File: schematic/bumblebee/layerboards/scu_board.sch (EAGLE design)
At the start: 15 parts, among them P5 B4B-EH-A, P7 B3B-EH-A

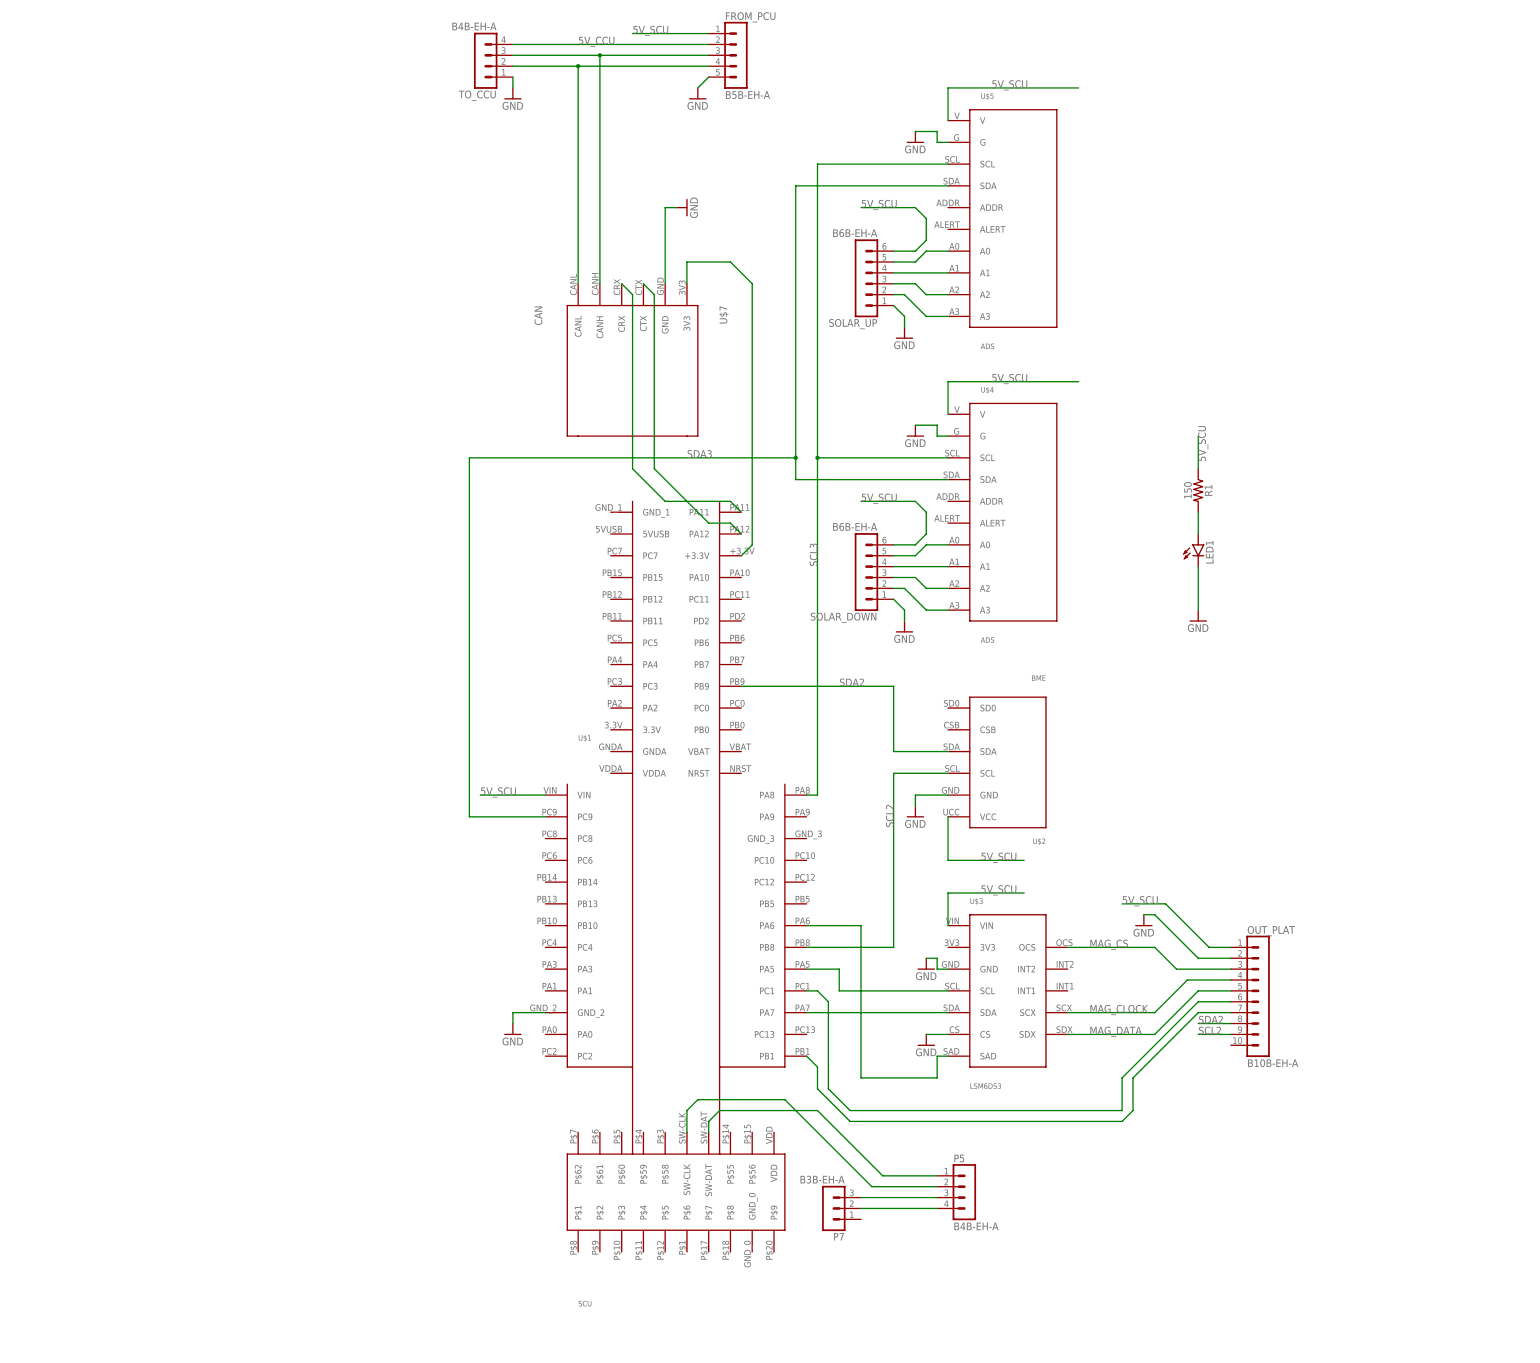
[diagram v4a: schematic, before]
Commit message: ICU готова, SCU скоро доделаю, пока что там всё не очень В либу добавлен LSM303C
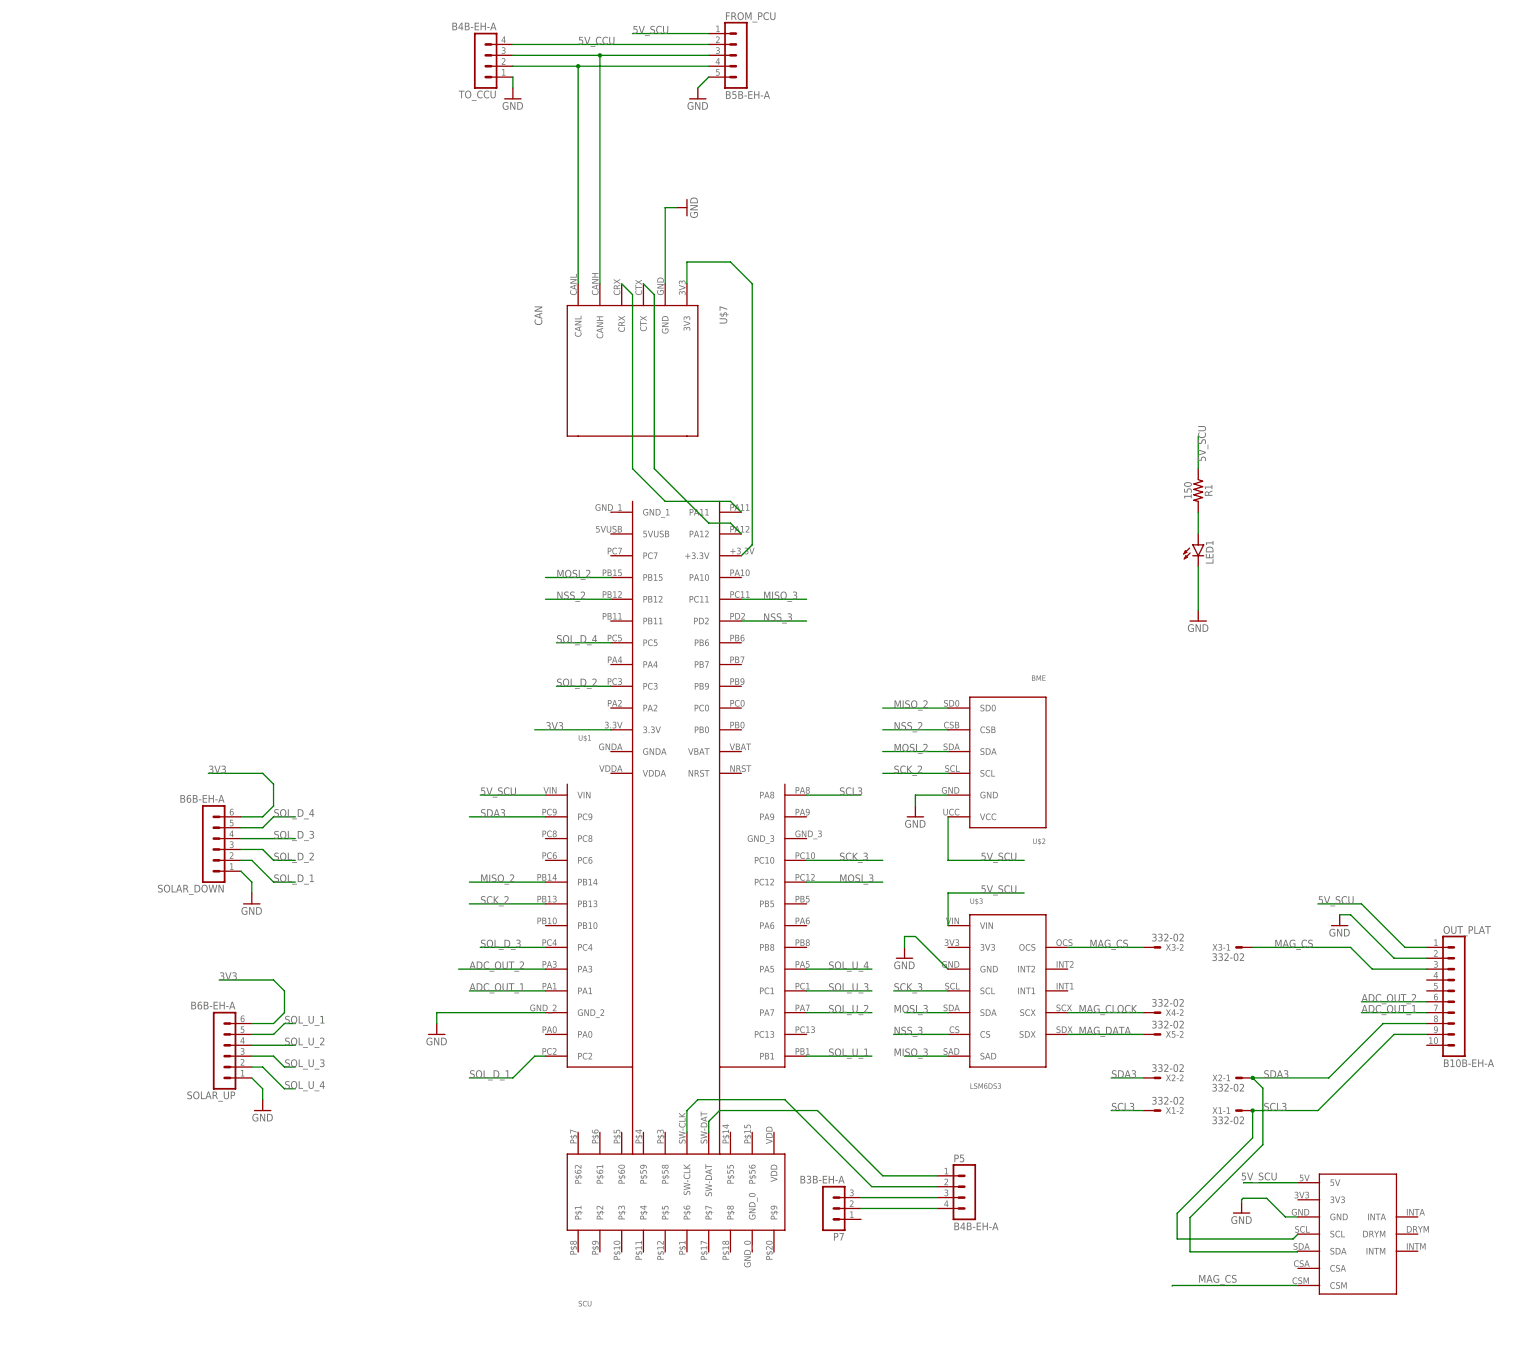
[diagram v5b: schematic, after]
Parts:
- removed U$5: ADS, bluepill:ADS
- added X1, X2, X3, X4, X5: 332-02, con-garry:332-02
- U$4: value ADS -> LSM303C; device bluepill:ADS -> bluepill:LSM303C
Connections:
- removed net N$10: SOLAR_UP.3, U$5.A2
- removed net N$11: SOLAR_UP.2, U$5.A3
- removed net N$12: SOLAR_DOWN.5, U$4.A0
- removed net N$13: SOLAR_DOWN.4, U$4.A1
- removed net N$14: SOLAR_DOWN.3, U$4.A2
- removed net N$15: SOLAR_DOWN.2, U$4.A3
- removed net N$17: OUT_PLAT.6, U$1.PC1
- removed net N$18: OUT_PLAT.7, U$1.PB1
- removed net N$2: U$1.PA5, U$3.SCL
- removed net N$3: U$1.PA6, U$3.SAD
- removed net N$4: U$1.PA7, U$3.SDA
- removed net N$8: SOLAR_UP.5, U$5.A0
- removed net N$9: SOLAR_UP.4, U$5.A1
- removed net SCL2: OUT_PLAT.9, U$1.PB8, U$2.SCL
- removed net SDA2: OUT_PLAT.8, U$1.PB9, U$2.SDA
- new net 3V3: SOLAR_DOWN.6, SOLAR_UP.6, U$1.3.3V
- new net ADC_OUT_1: OUT_PLAT.7, U$1.PA1
- new net ADC_OUT_2: OUT_PLAT.6, U$1.PA3
- new net MISO_2: U$1.PB14, U$2.SD0
- new net MISO_3: U$1.PC11, U$3.SAD
- new net MOSI_2: U$1.PB15, U$2.SDA
- new net MOSI_3: U$1.PC12, U$3.SDA
- new net NSS_2: U$1.PB12, U$2.CSB
- new net NSS_3: U$1.PD2, U$3.CS
- new net SCK_2: U$1.PB13, U$2.SCL
- new net SCK_3: U$1.PC10, U$3.SCL
- new net SOL_D_1: SOLAR_DOWN.2, U$1.PC2
- new net SOL_D_2: SOLAR_DOWN.3, U$1.PC3
- new net SOL_D_3: SOLAR_DOWN.4, U$1.PC4
- new net SOL_D_4: SOLAR_DOWN.5, U$1.PC5
- new net SOL_U_1: SOLAR_UP.5, U$1.PB1
- new net SOL_U_2: SOLAR_UP.4, U$1.PA7
- new net SOL_U_3: SOLAR_UP.3, U$1.PC1
- new net SOL_U_4: SOLAR_UP.2, U$1.PA5
- net 5V_SCU: now also U$4.5V; no longer SOLAR_DOWN.6, SOLAR_UP.6, U$4.V, U$5.V
- net GND: now also U$4.GND; no longer U$3.CS, U$4.G, U$5.G
- net MAG_CLOCK: now also X4-2.S; no longer OUT_PLAT.4
- net MAG_CS: now also U$4.CSM, X3-1.S, X3-2.S
- net MAG_DATA: now also X5-2.S; no longer OUT_PLAT.5
- net SCL3: now also OUT_PLAT.9, X1-1.S, X1-2.S; no longer U$5.SCL
- net SDA3: now also OUT_PLAT.8, X2-1.S, X2-2.S; no longer U$5.SDA
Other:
- moved on the sheet: OUT_PLAT, SOLAR_DOWN, SOLAR_UP

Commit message: Готова SCU и поправил lsm303c в либе
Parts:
- removed OUT_PLAT: B10B-EH-A, con-jst-eh:B10B-EH-A
- removed X1, X2, X3, X4, X5: 332-02, con-garry:332-02
- added P1: B8B-EH-A, con-jst-eh:B8B-EH-A
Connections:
- removed net MAG_CLOCK: U$3.SCX, X4-2.S
- removed net MAG_DATA: U$3.SDX, X5-2.S
- net 5V_SCU: now also P1.1; no longer OUT_PLAT.1
- net ADC_OUT_1: now also P1.5; no longer OUT_PLAT.7
- net ADC_OUT_2: now also P1.4; no longer OUT_PLAT.6
- net GND: now also P1.2; no longer OUT_PLAT.2
- net MAG_CS: now also P1.3; no longer OUT_PLAT.3, X3-1.S, X3-2.S
- net SCL3: now also P1.7, U$3.SCX; no longer OUT_PLAT.9, X1-1.S, X1-2.S
- net SDA3: now also P1.6, U$3.SDX; no longer OUT_PLAT.8, X2-1.S, X2-2.S

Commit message: Подготовка плат к производству
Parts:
- removed SOLAR_DOWN, SOLAR_UP: B6B-EH-A, con-jst-eh:B6B-EH-A
- added R2, R3, R4, R5, R6, R7, R8, R9: 150, SparkFun-Resistors:RESISTORAXIAL-0.3
- added SOL_D_1_2, SOL_D_3_4, SOL_U_1_2, SOL_U_3_4: B4B-EH-A, con-jst-eh:B4B-EH-A
- renumbered P1 to TO_OUT_BOARD, P5 to DEBUG, P7 to DEBUG_OUT
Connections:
- net 3V3: now also SOL_D_1_2.2, SOL_D_1_2.4, SOL_D_3_4.2, SOL_D_3_4.4, SOL_U_1_2.2, SOL_U_1_2.4, SOL_U_3_4.2, SOL_U_3_4.4; no longer SOLAR_DOWN.6, SOLAR_UP.6
- net GND: now also R2.1, R3.1, R4.2, R5.1, R6.1, R7.2, R8.2, R9.1; no longer SOLAR_DOWN.1, SOLAR_UP.1
- net SOL_D_1: now also R9.2, SOL_D_1_2.1; no longer SOLAR_DOWN.2
- net SOL_D_2: now also R8.1, SOL_D_1_2.3; no longer SOLAR_DOWN.3
- net SOL_D_3: now also R7.1, SOL_D_3_4.1; no longer SOLAR_DOWN.4
- net SOL_D_4: now also R6.2, SOL_D_3_4.3; no longer SOLAR_DOWN.5
- net SOL_U_1: now also R5.2, SOL_U_1_2.1; no longer SOLAR_UP.5
- net SOL_U_2: now also R4.1, SOL_U_1_2.3; no longer SOLAR_UP.4
- net SOL_U_3: now also R3.2, SOL_U_3_4.1; no longer SOLAR_UP.3
- net SOL_U_4: now also R2.2, SOL_U_3_4.3; no longer SOLAR_UP.2

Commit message: Платы отправлены на завод
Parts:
- renumbered U$1 to STM32H405
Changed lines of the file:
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@@
 </classes>
 <parts>
-<part name="U$1" library="bluepill" deviceset="SCU" device=""/>
+<part name="STM32H405" library="bluepill" deviceset="SCU" device=""/>
 <part name="U$2" library="bluepill" deviceset="BME" device=""/>
 <part name="GND1" library="supply1" library_urn="urn:adsk.eagle:library:371" deviceset="GND" device=""/>
@@
 </plain>
 <instances>
-<instance part="U$1" gate="G$1" x="5.08" y="2.54" smashed="yes">
+<instance part="STM32H405" gate="G$1" x="5.08" y="2.54" smashed="yes">
 <attribute name="NAME" x="-22.86" y="53.34" size="1.27" layer="95"/>
 <attribute name="VALUE" x="-22.86" y="-78.74" size="1.27" layer="96"/>
@@
 <segment>
 <pinref part="GND2" gate="1" pin="GND"/>
-<pinref part="U$1" gate="G$1" pin="GND_2"/>
+<pinref part="STM32H405" gate="G$1" pin="GND_2"/>
 <wire x1="-55.88" y1="-12.7" x2="-55.88" y2="-10.16" width="0.1524" layer="91"/>
 <wire x1="-55.88" y1="-10.16" x2="-30.48" y2="-10.16" width="0.1524" layer="91"/>
@@
 </segment>
 <segment>
-<pinref part="U$1" gate="G$1" pin="VIN"/>
+<pinref part="STM32H405" gate="G$1" pin="VIN"/>
 <wire x1="-30.48" y1="40.64" x2="-45.72" y2="40.64" width="0.1524" layer="91"/>
 <label x="-45.72" y="40.64" size="1.778" layer="95"/>
@@
 <net name="SCL3" class="0">
 <segment>
-<pinref part="U$1" gate="G$1" pin="PA8"/>
+<pinref part="STM32H405" gate="G$1" pin="PA8"/>
 <label x="38.1" y="40.64" size="1.778" layer="95"/>
 <wire x1="30.48" y1="40.64" x2="43.18" y2="40.64" width="0.1524" layer="91"/>
@@
 <net name="SDA3" class="0">
 <segment>
-<pinref part="U$1" gate="G$1" pin="PC9"/>
+<pinref part="STM32H405" gate="G$1" pin="PC9"/>
 <wire x1="-30.48" y1="35.56" x2="-48.26" y2="35.56" width="0.1524" layer="91"/>
 <label x="-45.72" y="35.56" size="1.778" layer="95"/>
@@
 <net name="ADC_OUT_1" class="0">
 <segment>
-<pinref part="U$1" gate="G$1" pin="PA1"/>
+<pinref part="STM32H405" gate="G$1" pin="PA1"/>
 <wire x1="-30.48" y1="-5.08" x2="-48.26" y2="-5.08" width="0.1524" layer="91"/>
 <label x="-48.26" y="-5.08" size="1.778" layer="95"/>
@@
 <net name="N$22" class="0">
 <segment>
-<pinref part="U$1" gate="G$1" pin="SW-DAT"/>
+<pinref part="STM32H405" gate="G$1" pin="SW-DAT"/>
 <wire x1="7.62" y1="-38.1" x2="7.62" y2="-35.56" width="0.1524" layer="91"/>
 <wire x1="7.62" y1="-35.56" x2="10.16" y2="-33.02" width="0.1524" layer="91"/>
@@
 <wire x1="25.4" y1="-30.48" x2="5.08" y2="-30.48" width="0.1524" layer="91"/>
 <wire x1="5.08" y1="-30.48" x2="2.54" y2="-33.02" width="0.1524" layer="91"/>
-<pinref part="U$1" gate="G$1" pin="SW-CLK"/>
+<pinref part="STM32H405" gate="G$1" pin="SW-CLK"/>
 <wire x1="2.54" y1="-33.02" x2="2.54" y2="-38.1" width="0.1524" layer="91"/>
 </segment>
@@
 <wire x1="-10.16" y1="116.84" x2="-2.54" y2="109.22" width="0.1524" layer="91"/>
 <wire x1="-2.54" y1="109.22" x2="12.7" y2="109.22" width="0.1524" layer="91"/>
-<pinref part="U$1" gate="G$1" pin="PA11"/>
+<pinref part="STM32H405" gate="G$1" pin="PA11"/>
 <wire x1="12.7" y1="109.22" x2="15.24" y2="106.68" width="0.1524" layer="91"/>
 </segment>
@@
 <net name="N$7" class="0">
 <segment>
-<pinref part="U$1" gate="G$1" pin="PA12"/>
+<pinref part="STM32H405" gate="G$1" pin="PA12"/>
 <wire x1="15.24" y1="101.6" x2="12.7" y2="104.14" width="0.1524" layer="91"/>
 <wire x1="12.7" y1="104.14" x2="7.62" y2="104.14" width="0.1524" layer="91"/>
@@
 <net name="N$16" class="0">
 <segment>
-<pinref part="U$1" gate="G$1" pin="+3.3V"/>
+<pinref part="STM32H405" gate="G$1" pin="+3.3V"/>
 <wire x1="15.24" y1="96.52" x2="17.78" y2="99.06" width="0.1524" layer="91"/>
 <wire x1="17.78" y1="99.06" x2="17.78" y2="160.02" width="0.1524" layer="91"/>
@@
 <net name="SOL_D_2" class="0">
 <segment>
-<pinref part="U$1" gate="G$1" pin="PC3"/>
+<pinref part="STM32H405" gate="G$1" pin="PC3"/>
 <wire x1="-15.24" y1="66.04" x2="-27.94" y2="66.04" width="0.1524" layer="91"/>
 <label x="-27.94" y="66.04" size="1.778" layer="95"/>
@@
 <net name="SOL_D_3" class="0">
 <segment>
-<pinref part="U$1" gate="G$1" pin="PC4"/>
+<pinref part="STM32H405" gate="G$1" pin="PC4"/>
 <wire x1="-30.48" y1="5.08" x2="-45.72" y2="5.08" width="0.1524" layer="91"/>
 <label x="-45.72" y="5.08" size="1.778" layer="95"/>
@@
 <net name="SOL_D_4" class="0">
 <segment>
-<pinref part="U$1" gate="G$1" pin="PC5"/>
+<pinref part="STM32H405" gate="G$1" pin="PC5"/>
 <wire x1="-15.24" y1="76.2" x2="-27.94" y2="76.2" width="0.1524" layer="91"/>
 <label x="-27.94" y="76.2" size="1.778" layer="95"/>
@@
 <net name="3V3" class="0">
 <segment>
-<pinref part="U$1" gate="G$1" pin="3.3V"/>
+<pinref part="STM32H405" gate="G$1" pin="3.3V"/>
 <wire x1="-15.24" y1="55.88" x2="-33.02" y2="55.88" width="0.1524" layer="91"/>
 <label x="-30.48" y="55.88" size="1.778" layer="95"/>
@@
 <net name="ADC_OUT_2" class="0">
 <segment>
-<pinref part="U$1" gate="G$1" pin="PA3"/>
+<pinref part="STM32H405" gate="G$1" pin="PA3"/>
 <wire x1="-30.48" y1="0" x2="-50.8" y2="0" width="0.1524" layer="91"/>
 <label x="-48.26" y="0" size="1.778" layer="95"/>
@@
 </segment>
 <segment>
-<pinref part="U$1" gate="G$1" pin="PB12"/>
+<pinref part="STM32H405" gate="G$1" pin="PB12"/>
 <wire x1="-15.24" y1="86.36" x2="-30.48" y2="86.36" width="0.1524" layer="91"/>
 <label x="-27.94" y="86.36" size="1.778" layer="95"/>
@@
 </segment>
 <segment>
-<pinref part="U$1" gate="G$1" pin="PB15"/>
+<pinref part="STM32H405" gate="G$1" pin="PB15"/>
 <wire x1="-15.24" y1="91.44" x2="-30.48" y2="91.44" width="0.1524" layer="91"/>
 <label x="-27.94" y="91.44" size="1.778" layer="95"/>
@@
 </segment>
 <segment>
-<pinref part="U$1" gate="G$1" pin="PB13"/>
+<pinref part="STM32H405" gate="G$1" pin="PB13"/>
 <wire x1="-30.48" y1="15.24" x2="-48.26" y2="15.24" width="0.1524" layer="91"/>
 <label x="-45.72" y="15.24" size="1.778" layer="95"/>
@@
 </segment>
 <segment>
-<pinref part="U$1" gate="G$1" pin="PB14"/>
+<pinref part="STM32H405" gate="G$1" pin="PB14"/>
 <wire x1="-30.48" y1="20.32" x2="-48.26" y2="20.32" width="0.1524" layer="91"/>
 <label x="-45.72" y="20.32" size="1.778" layer="95"/>
@@
 <net name="SCK_3" class="0">
 <segment>
-<pinref part="U$1" gate="G$1" pin="PC10"/>
+<pinref part="STM32H405" gate="G$1" pin="PC10"/>
 <wire x1="30.48" y1="25.4" x2="48.26" y2="25.4" width="0.1524" layer="91"/>
 <label x="38.1" y="25.4" size="1.778" layer="95"/>
@@
 <net name="MOSI_3" class="0">
 <segment>
-<pinref part="U$1" gate="G$1" pin="PC12"/>
+<pinref part="STM32H405" gate="G$1" pin="PC12"/>
 <wire x1="30.48" y1="20.32" x2="48.26" y2="20.32" width="0.1524" layer="91"/>
 <label x="38.1" y="20.32" size="1.778" layer="95"/>
@@
 <net name="MISO_3" class="0">
 <segment>
-<pinref part="U$1" gate="G$1" pin="PC11"/>
+<pinref part="STM32H405" gate="G$1" pin="PC11"/>
 <wire x1="15.24" y1="86.36" x2="30.48" y2="86.36" width="0.1524" layer="91"/>
 <label x="20.32" y="86.36" size="1.778" layer="95"/>
@@
 <net name="NSS_3" class="0">
 <segment>
-<pinref part="U$1" gate="G$1" pin="PD2"/>
+<pinref part="STM32H405" gate="G$1" pin="PD2"/>
 <wire x1="15.24" y1="81.28" x2="30.48" y2="81.28" width="0.1524" layer="91"/>
 <label x="20.32" y="81.28" size="1.778" layer="95"/>
@@
 </segment>
 <segment>
-<pinref part="U$1" gate="G$1" pin="PA5"/>
+<pinref part="STM32H405" gate="G$1" pin="PA5"/>
 <wire x1="30.48" y1="0" x2="45.72" y2="0" width="0.1524" layer="91"/>
 <label x="35.56" y="0" size="1.778" layer="95"/>
@@
 </segment>
 <segment>
-<pinref part="U$1" gate="G$1" pin="PC1"/>
+<pinref part="STM32H405" gate="G$1" pin="PC1"/>
 <wire x1="30.48" y1="-5.08" x2="45.72" y2="-5.08" width="0.1524" layer="91"/>
 <label x="35.56" y="-5.08" size="1.778" layer="95"/>
@@
 </segment>
 <segment>
-<pinref part="U$1" gate="G$1" pin="PA7"/>
+<pinref part="STM32H405" gate="G$1" pin="PA7"/>
 <wire x1="30.48" y1="-10.16" x2="45.72" y2="-10.16" width="0.1524" layer="91"/>
 <label x="35.56" y="-10.16" size="1.778" layer="95"/>
@@
 </segment>
 <segment>
-<pinref part="U$1" gate="G$1" pin="PB1"/>
+<pinref part="STM32H405" gate="G$1" pin="PB1"/>
 <wire x1="30.48" y1="-20.32" x2="45.72" y2="-20.32" width="0.1524" layer="91"/>
 <label x="35.56" y="-20.32" size="1.778" layer="95"/>
@@
 </segment>
 <segment>
-<pinref part="U$1" gate="G$1" pin="PC2"/>
+<pinref part="STM32H405" gate="G$1" pin="PC2"/>
 <wire x1="-30.48" y1="-20.32" x2="-33.02" y2="-20.32" width="0.1524" layer="91"/>
 <wire x1="-33.02" y1="-20.32" x2="-38.1" y2="-25.4" width="0.1524" layer="91"/>
